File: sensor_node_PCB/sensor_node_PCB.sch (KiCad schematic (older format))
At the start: 33 parts, among them J1 USB_B_Mini, J3 OUTPUT_CONNECTOR, P1 BREAKOUTS, Q1 FDN340P, Q2 BSS138, Q3 BSS138, U1 LMV358IDGKR, U10 dps310, U2 LD1117S50TR, U3 FT231XS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

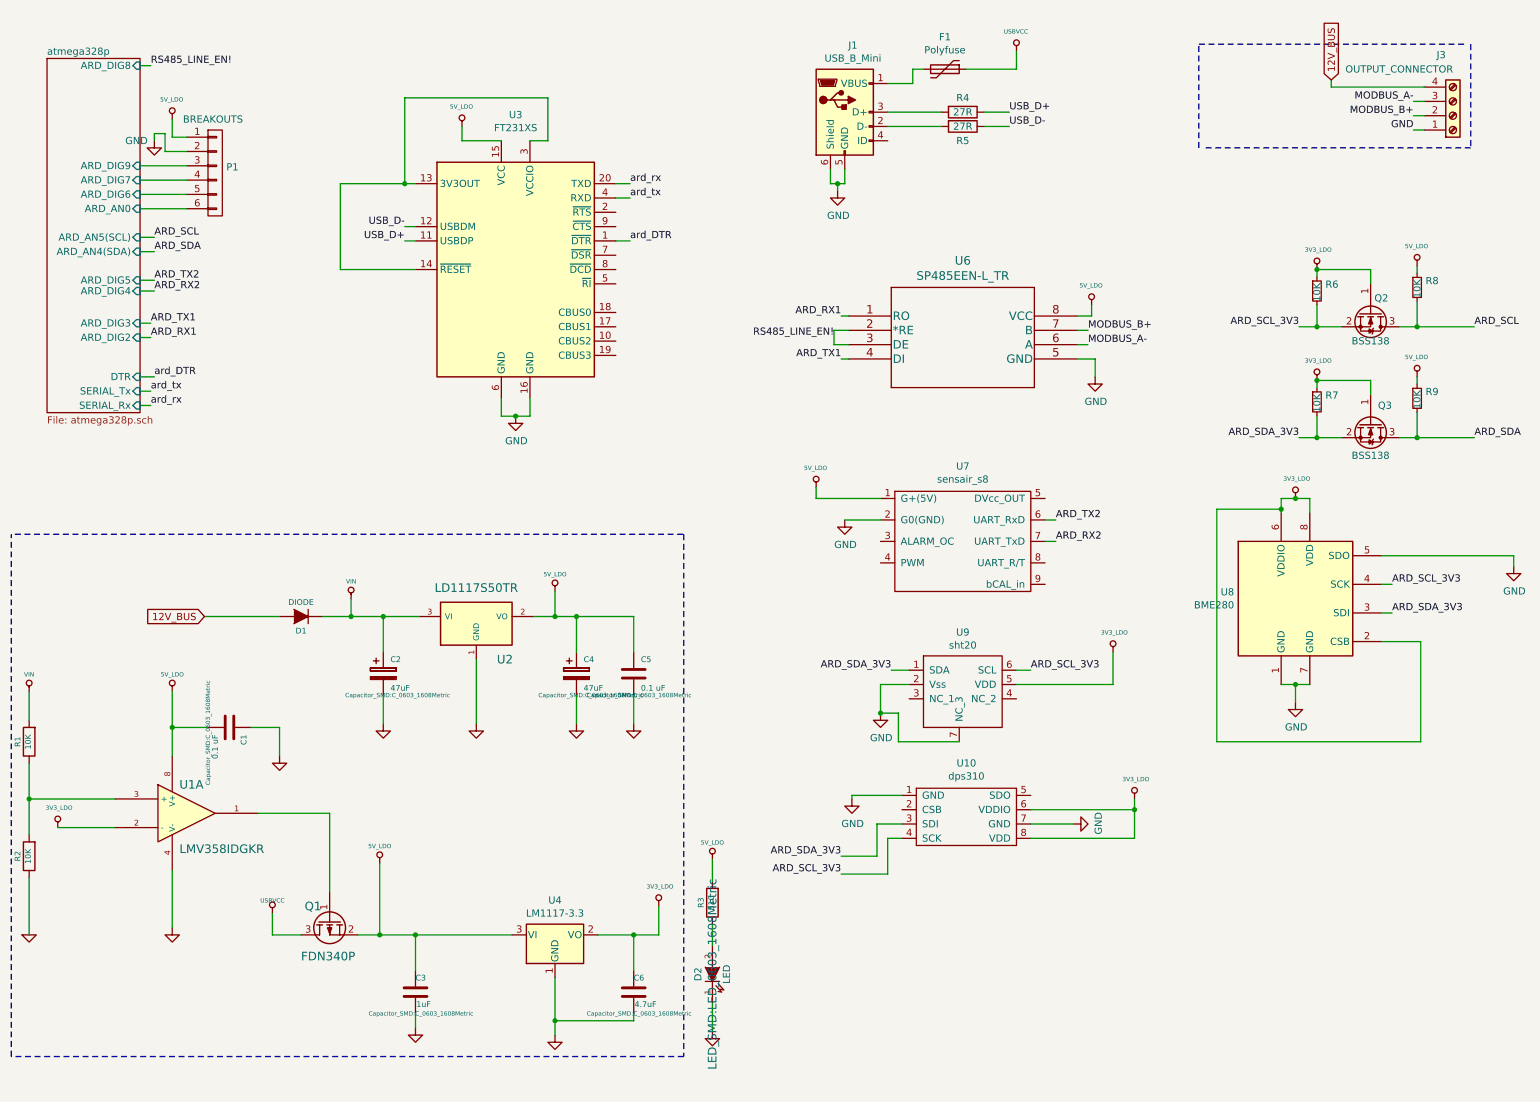
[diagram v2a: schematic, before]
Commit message: changed usb ic to cp2102 on schematic
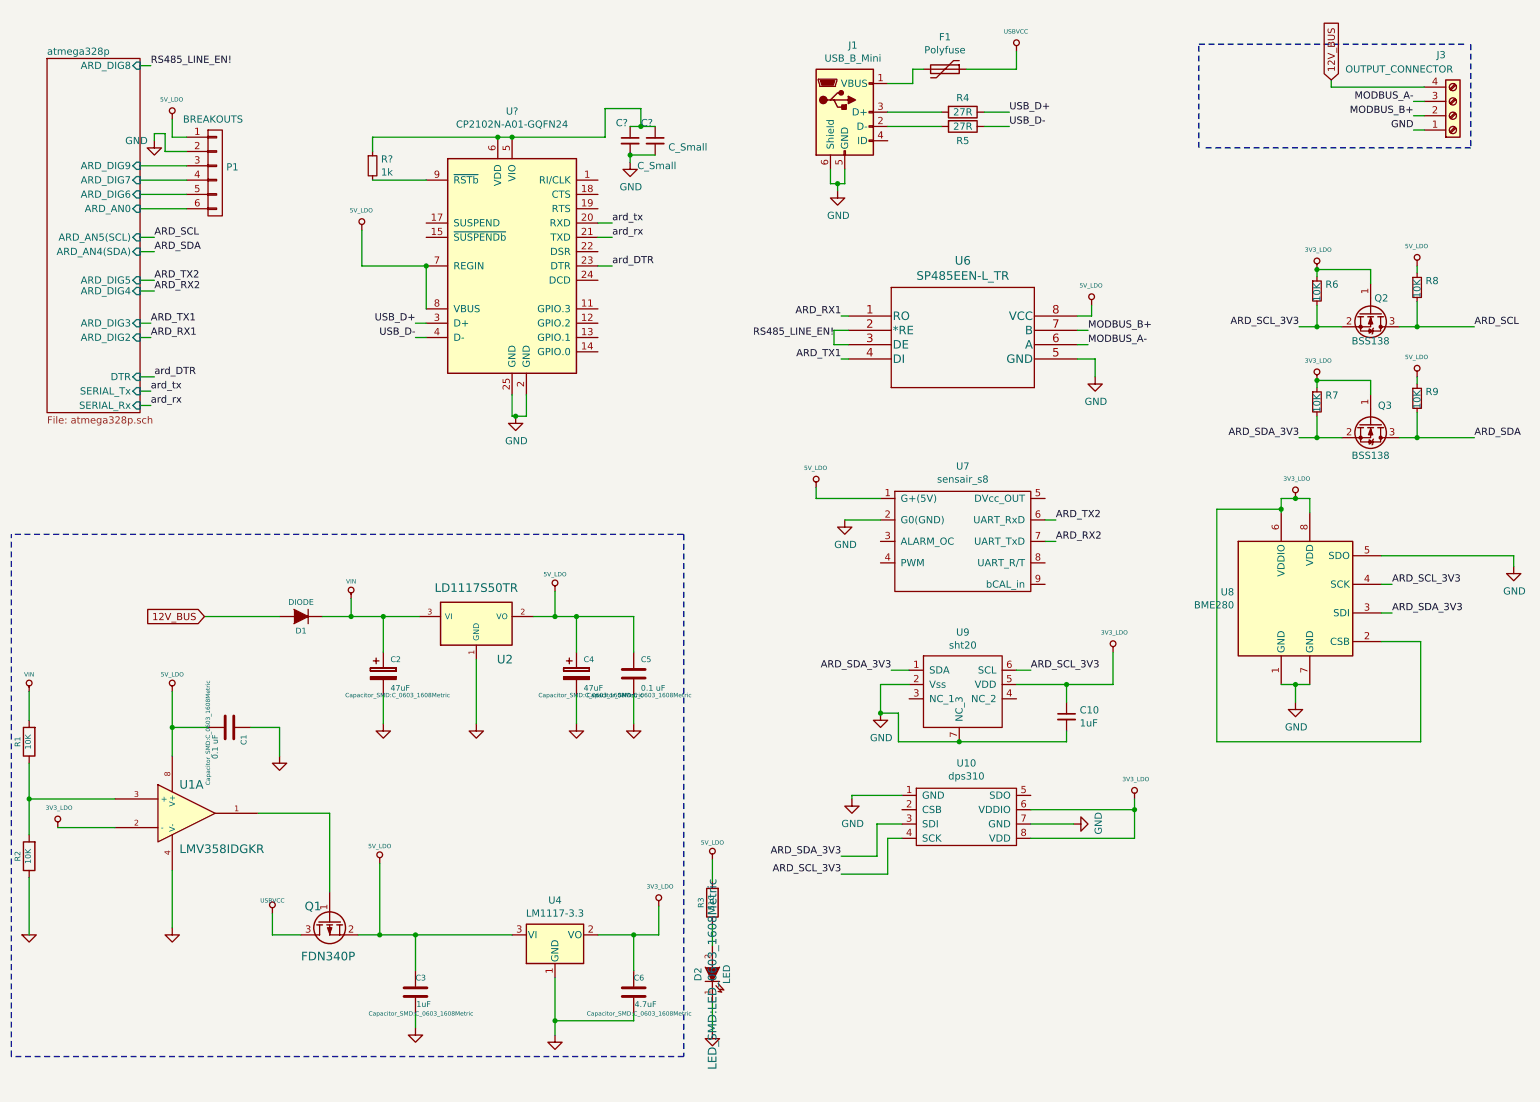
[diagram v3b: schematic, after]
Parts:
- removed U3: FT231XS, Package_SO:SSOP-20_3.9x8.7mm_P0.635mm, symbol Interface_USB:FT231XS
- added C10: 1uF, Capacitor_SMD:C_0603_1608Metric, symbol Device:C_Small
- added C? (x2): C_Small, symbol Device:C_Small
- added R?: 1k, symbol Device:R_Small
- added U?: CP2102N-A01-GQFN24, Package_DFN_QFN:QFN-24-1EP_4x4mm_P0.5mm_EP2.6x2.6mm, symbol Interface_USB:CP2102N-A01-GQFN24
- P1: footprint TerminalBlock_Phoenix:TerminalBlock_Phoenix_MPT-0,5-6-2.54_1x06_P2.54mm_Horizontal -> TerminalBlock:TerminalBlock_bornier-6_P5.08mm
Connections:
- net 3V3_LDO: now also C10.1
- net 5V_LDO: now also U?.7 (REGIN), U?.8 (VBUS)
- net GND: now also C10.2, C?.2, C?.2, U?.2 (GND), U?.25 (GND)
- net USB_D+: now also U?.3 (D+)
- net USB_D-: now also U?.4 (D-)
- net ard_DTR: now also U?.23 (DTR)
- net ard_rx: now also U?.21 (TXD)
- net ard_tx: now also U?.20 (RXD)
- new net: C?.1, C?.1, R?.1, U?.5 (VIO), U?.6 (VDD)
- new net: R?.2, U?.9 (~RSTb)
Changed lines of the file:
@@
 Text GLabel 1800 4725 0    50   Input ~ 0
 12V_BUS
-$Comp
-L Interface_USB:FT231XS U3
-U 1 1 5F4E39B1
-P 3975 2300
-F 0 "U3" H 3975 3381 50  0000 C CNN
-F 1 "FT231XS" H 3975 3290 50  0000 C CNN
-F 2 "Package_SO:SSOP-20_3.9x8.7mm_P0.635mm" H 4975 1500 50  0001 C CNN
-F 3 "https://www.ftdichip.com/Support/Documents/DataSheets/ICs/DS_FT231X.pdf" H 3975 2300 50  0001 C CNN
-	1    3975 2300
-	1    0    0    -1
-$EndComp
-Text Label 3200 2100 2    50   ~ 0
+Text Label 3275 2675 2    50   ~ 0
 USB_D+
-Text Label 3200 2000 2    50   ~ 0
+Text Label 3275 2775 2    50   ~ 0
 USB_D-
-Wire Wire Line
-	3200 2000 3275 2000
-Wire Wire Line
-	3200 2100 3275 2100
-$Comp
-L Arduino_Uno_R3_From_Scratch-rescue:5V_LDO #PWR0111
-U 1 1 5F4ED2A9
-P 3600 1300
-F 0 "#PWR0111" H 3600 1390 20  0001 C CNN
-F 1 "5V_LDO" H 3596 1438 30  0000 C CNN
-F 2 "" H 3600 1300 60  0000 C CNN
-F 3 "" H 3600 1300 60  0000 C CNN
-	1    3600 1300
-	1    0    0    -1
-$EndComp
 Text Label 1425 3150 0    50   ~ 0
 ard_tx
@@
 Wire Wire Line
 	1350 3250 1425 3250
-Text Label 4775 1800 0    50   ~ 0
+Text Label 4650 1975 0    50   ~ 0
 ard_tx
-Text Label 4775 1700 0    50   ~ 0
+Text Label 4650 2075 0    50   ~ 0
 ard_rx
-Wire Wire Line
-	4675 1700 4775 1700
-Wire Wire Line
-	4675 1800 4775 1800
 Text Label 1450 3050 0    50   ~ 0
 ard_DTR
-Text Label 4775 2100 0    50   ~ 0
+Text Label 4650 2275 0    50   ~ 0
 ard_DTR
-Wire Wire Line
-	4675 2100 4775 2100
 $Comp
 L Arduino_Uno_R3_From_Scratch-rescue:GND #PWR0112
@@
 	1    0    0    -1
 $EndComp
-Wire Wire Line
-	3875 3200 3875 3325
-Wire Wire Line
-	3875 3325 3975 3325
-Wire Wire Line
-	4075 3200 4075 3325
-Wire Wire Line
-	4075 3325 3975 3325
-Connection ~ 3975 3325
-Wire Wire Line
-	3600 1300 3600 1400
-Wire Wire Line
-	3600 1400 3875 1400
-Wire Wire Line
-	3275 1700 3200 1700
-Wire Wire Line
-	3200 1700 3200 1100
-Wire Wire Line
-	3200 1100 4200 1100
-Wire Wire Line
-	4200 1100 4200 1400
-Wire Wire Line
-	4200 1400 4075 1400
 Text Label 1425 2675 0    50   ~ 0
 ARD_TX1
@@
 F 0 "P1" H 1953 1666 50  0000 L CNN
 F 1 "BREAKOUTS" H 1650 2000 50  0000 L CNN
-F 2 "TerminalBlock_Phoenix:TerminalBlock_Phoenix_MPT-0,5-6-2.54_1x06_P2.54mm_Horizontal" H 1875 1625 60  0001 C CNN
+F 2 "TerminalBlock:TerminalBlock_bornier-6_P5.08mm" H 1875 1625 60  0001 C CNN
 F 3 "" H 1875 1625 60  0000 C CNN
 	1    1875 1625
@@
 F15 "ARD_DIG9" I R 1350 1575 50
 $EndSheet
-Wire Wire Line
-	3275 2300 2750 2300
-Wire Wire Line
-	2750 2300 2750 1700
-Wire Wire Line
-	2750 1700 3200 1700
-Connection ~ 3200 1700
 $Comp
 L Arduino_Uno_R3_From_Scratch-rescue:R R?
@@
 	8150 4975 8150 5200
 Wire Wire Line
-	8150 5200 7475 5200
+	8150 5200 7825 5200
 $Comp
 L Kicad_symbols:dps310 U10
@@
 	6650 5400 6525 5400
 Connection ~ 6525 5400
+$Comp
+L Device:C_Small C10
+U 1 1 5FE85087
+P 7825 5425
+F 0 "C10" H 7917 5471 50  0000 L CNN
+F 1 "1uF" H 7917 5380 50  0000 L CNN
+F 2 "Capacitor_SMD:C_0603_1608Metric" H 7825 5425 50  0001 C CNN
+F 3 "~" H 7825 5425 50  0001 C CNN
+	1    7825 5425
+	1    0    0    -1
+$EndComp
+Wire Wire Line
+	7825 5200 7825 5325
+Connection ~ 7825 5200
+Wire Wire Line
+	7825 5200 7475 5200
+Wire Wire Line
+	7825 5525 7825 5600
+Wire Wire Line
+	7825 5600 7075 5600
+Connection ~ 7075 5600
+$Comp
+L Interface_USB:CP2102N-A01-GQFN24 U?
+U 1 1 5FEADE93
+P 3950 2275
+F 0 "U?" H 3950 3356 50  0000 C CNN
+F 1 "CP2102N-A01-GQFN24" H 3950 3265 50  0000 C CNN
+F 2 "Package_DFN_QFN:QFN-24-1EP_4x4mm_P0.5mm_EP2.6x2.6mm" H 4400 1475 50  0001 L CNN
+F 3 "https://www.silabs.com/documents/public/data-sheets/cp2102n-datasheet.pdf" H 4000 1225 50  0001 C CNN
+	1    3950 2275
+	1    0    0    -1
+$EndComp
+$Comp
+L Arduino_Uno_R3_From_Scratch-rescue:5V_LDO #PWR?
+U 1 1 5FEB97F5
+P 2900 2025
+F 0 "#PWR?" H 2900 2115 20  0001 C CNN
+F 1 "5V_LDO" H 2896 2163 30  0000 C CNN
+F 2 "" H 2900 2025 60  0000 C CNN
+F 3 "" H 2900 2025 60  0000 C CNN
+	1    2900 2025
+	1    0    0    -1
+$EndComp
+Wire Wire Line
+	2900 2025 2900 2275
+Wire Wire Line
+	2900 2275 3350 2275
+Wire Wire Line
+	3950 3175 3950 3325
+Wire Wire Line
+	3950 3325 3975 3325
+Wire Wire Line
+	4050 3175 4050 3325
+Wire Wire Line
+	4050 3325 3975 3325
+Connection ~ 3975 3325
+Wire Wire Line
+	4550 2275 4650 2275
+Wire Wire Line
+	4550 1975 4650 1975
+Wire Wire Line
+	4550 2075 4650 2075
+Wire Wire Line
+	3275 2675 3350 2675
+Wire Wire Line
+	3275 2775 3350 2775
+Wire Wire Line
+	3950 1375 3850 1375
+$Comp
+L Device:R_Small R?
+U 1 1 5FF181DD
+P 2975 1575
+F 0 "R?" H 3034 1621 50  0000 L CNN
+F 1 "1k" H 3034 1530 50  0000 L CNN
+F 2 "" H 2975 1575 50  0001 C CNN
+F 3 "~" H 2975 1575 50  0001 C CNN
+	1    2975 1575
+	1    0    0    -1
+$EndComp
+Wire Wire Line
+	2975 1675 3350 1675
+Wire Wire Line
+	2975 1375 3850 1375
+Wire Wire Line
+	2975 1375 2975 1475
+Connection ~ 3850 1375
+Wire Wire Line
+	3350 2575 3350 2275
+Connection ~ 3350 2275
+$Comp
+L Device:C_Small C?
+U 1 1 5FF3FE64
+P 4775 1400
+F 0 "C?" H 4675 1525 50  0000 L CNN
+F 1 "C_Small" H 4825 1225 50  0000 L CNN
+F 2 "" H 4775 1400 50  0001 C CNN
+F 3 "~" H 4775 1400 50  0001 C CNN
+	1    4775 1400
+	1    0    0    -1
+$EndComp
+$Comp
+L Device:C_Small C?
+U 1 1 5FF40686
+P 4950 1400
+F 0 "C?" H 4850 1525 50  0000 L CNN
+F 1 "C_Small" H 5042 1355 50  0000 L CNN
+F 2 "" H 4950 1400 50  0001 C CNN
+F 3 "~" H 4950 1400 50  0001 C CNN
+	1    4950 1400
+	1    0    0    -1
+$EndComp
+Wire Wire Line
+	3950 1375 4600 1375
+Wire Wire Line
+	4600 1375 4600 1175
+Wire Wire Line
+	4600 1175 4850 1175
+Wire Wire Line
+	4850 1175 4850 1300
+Wire Wire Line
+	4850 1300 4775 1300
+Connection ~ 3950 1375
+Wire Wire Line
+	4850 1300 4950 1300
+Connection ~ 4850 1300
+Wire Wire Line
+	4950 1500 4775 1500
+Wire Wire Line
+	4775 1500 4775 1550
+Connection ~ 4775 1500
+$Comp
+L Arduino_Uno_R3_From_Scratch-rescue:GND #PWR?
+U 1 1 5FF6DE1E
+P 4775 1550
+F 0 "#PWR?" H 4775 1300 50  0001 C CNN
+F 1 "GND" H 4780 1377 50  0000 C CNN
+F 2 "" H 4775 1550 60  0000 C CNN
+F 3 "" H 4775 1550 60  0000 C CNN
+	1    4775 1550
+	1    0    0    -1
+$EndComp
 $EndSCHEMATC
